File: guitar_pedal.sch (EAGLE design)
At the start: 97 parts, among them P1 RM-065, P2 RM-065, P3 RM-065, U1 LM324NSOIC-14, U2 LM324N, U3 LM386N-3, U4 LM386N-3, U5 LM386N-3

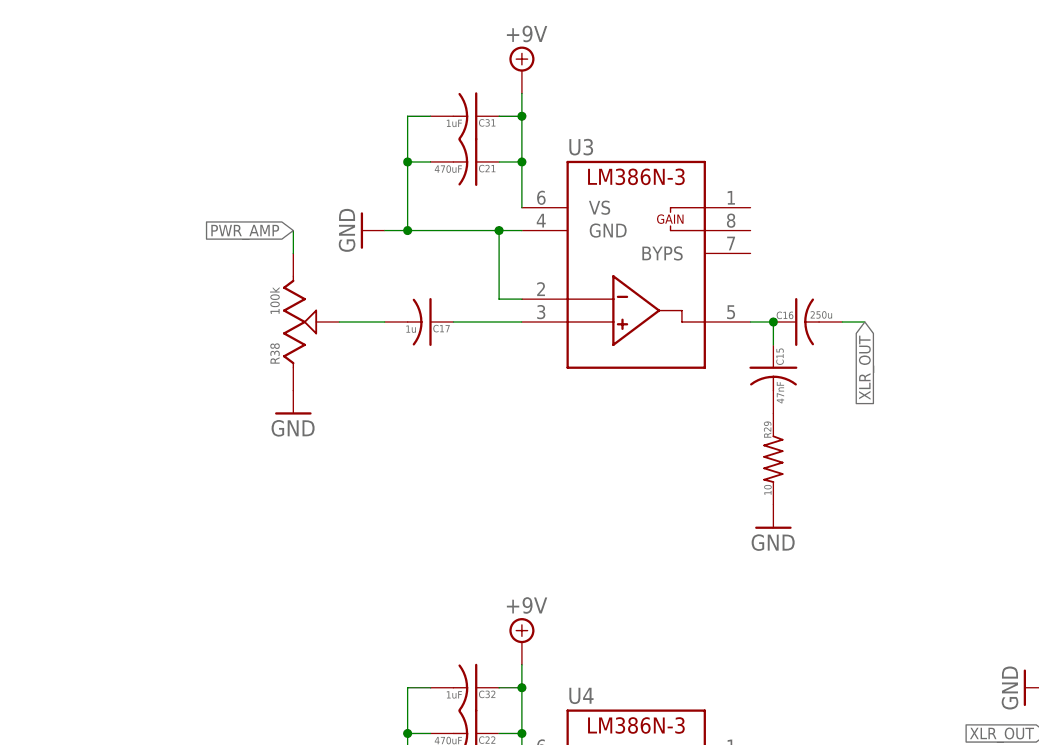
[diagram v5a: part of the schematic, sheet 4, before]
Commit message: Started layout. Placed output components.
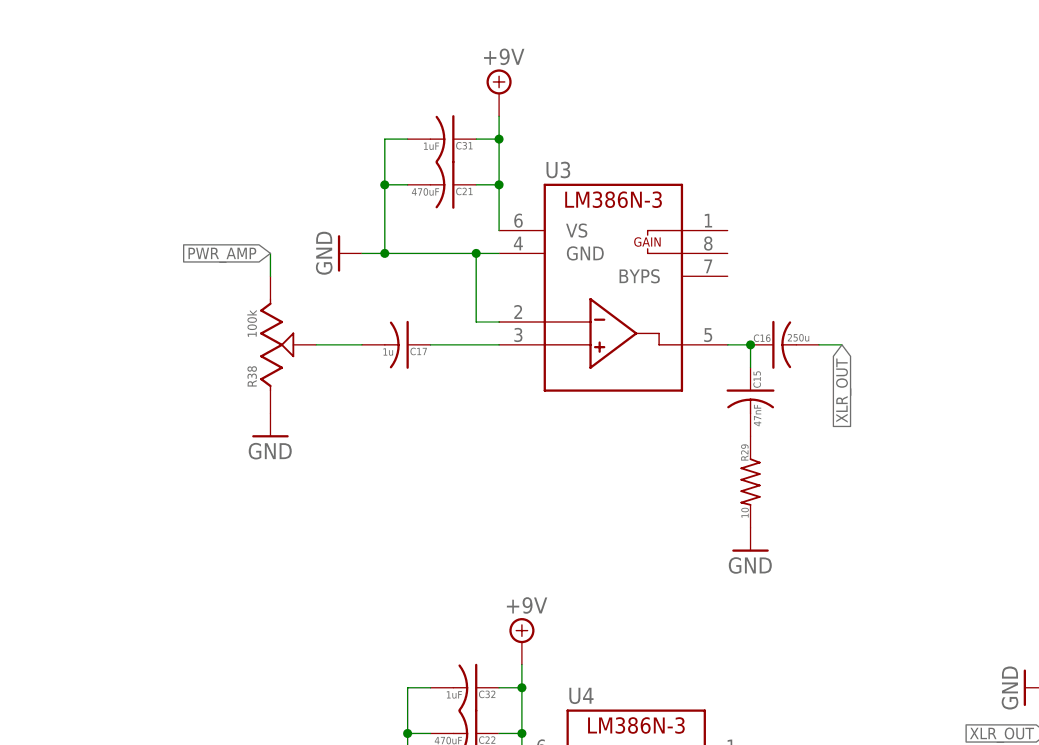
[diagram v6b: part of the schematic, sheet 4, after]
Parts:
- U2: value LM324N -> LM324NSOIC-14; device aarons:LM324N -> aarons:LM324NSOIC-14
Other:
- moved on the sheet: C15, C16, C17, C21, C31, R29, R38, U3
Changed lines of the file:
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@@
 <part name="C26" library="Luke" deviceset="CAP_CAN01" device="" value="470uF"/>
 <part name="U1" library="aarons" deviceset="LM324N" device="SOIC-14" value="LM324NSOIC-14"/>
-<part name="U2" library="aarons" deviceset="LM324N" device=""/>
+<part name="U2" library="aarons" deviceset="LM324N" device="SOIC-14" value="LM324NSOIC-14"/>
 <part name="FRAME2" library="frames" deviceset="FRAME_A_L" device="" value="Power"/>
 <part name="FRAME3" library="frames" deviceset="FRAME_A_L" device="" value="title"/>
@@
 <instance part="GND6" gate="1" x="218.44" y="121.92" rot="MR90"/>
 <instance part="GND7" gate="1" x="210.82" y="106.68" rot="MR90"/>
-<instance part="U3" gate="G$1" x="167.64" y="175.26"/>
-<instance part="GND29" gate="1" x="144.78" y="190.5" rot="R270"/>
-<instance part="C15" gate="G$1" x="190.5" y="175.26"/>
-<instance part="R29" gate="G$1" x="190.5" y="165.1" rot="R270"/>
-<instance part="C16" gate="G$1" x="193.04" y="180.34" rot="R90"/>
-<instance part="GND31" gate="1" x="190.5" y="157.48"/>
-<instance part="SUPPLY5" gate="G$1" x="162.56" y="208.28"/>
-<instance part="C17" gate="G$1" x="152.4" y="180.34" rot="R270"/>
-<instance part="GND32" gate="1" x="137.16" y="170.18"/>
+<instance part="U3" gate="G$1" x="165.1" y="172.72"/>
+<instance part="GND29" gate="1" x="142.24" y="187.96" rot="R270"/>
+<instance part="C15" gate="G$1" x="187.96" y="172.72"/>
+<instance part="R29" gate="G$1" x="187.96" y="162.56" rot="R270"/>
+<instance part="C16" gate="G$1" x="190.5" y="177.8" rot="R90"/>
+<instance part="GND31" gate="1" x="187.96" y="154.94"/>
+<instance part="SUPPLY5" gate="G$1" x="160.02" y="205.74"/>
+<instance part="C17" gate="G$1" x="149.86" y="177.8" rot="R270"/>
+<instance part="GND32" gate="1" x="134.62" y="167.64"/>
 <instance part="U4" gate="G$1" x="167.64" y="114.3"/>
 <instance part="GND33" gate="1" x="144.78" y="127" rot="R270"/>
@@
 <instance part="R36" gate="G$1" x="139.7" y="66.04"/>
 <instance part="R37" gate="G$1" x="137.16" y="119.38"/>
-<instance part="R38" gate="G$1" x="137.16" y="180.34"/>
-<instance part="C21" gate="G$1" x="157.48" y="198.12" rot="R270"/>
-<instance part="C31" gate="G$1" x="157.48" y="203.2" rot="R270"/>
+<instance part="R38" gate="G$1" x="134.62" y="177.8"/>
+<instance part="C21" gate="G$1" x="154.94" y="195.58" rot="R270"/>
+<instance part="C31" gate="G$1" x="154.94" y="200.66" rot="R270"/>
 <instance part="C32" gate="G$1" x="157.48" y="139.7" rot="R270"/>
 <instance part="C33" gate="G$1" x="157.48" y="86.36" rot="R270"/>
@@
 </segment>
 <segment>
-<wire x1="152.4" y1="198.12" x2="149.86" y2="198.12" width="0.1524" layer="91"/>
-<wire x1="149.86" y1="198.12" x2="149.86" y2="190.5" width="0.1524" layer="91"/>
+<wire x1="149.86" y1="195.58" x2="147.32" y2="195.58" width="0.1524" layer="91"/>
+<wire x1="147.32" y1="195.58" x2="147.32" y2="187.96" width="0.1524" layer="91"/>
 <pinref part="U3" gate="G$1" pin="GND"/>
-<wire x1="149.86" y1="190.5" x2="160.02" y2="190.5" width="0.1524" layer="91"/>
+<wire x1="147.32" y1="187.96" x2="157.48" y2="187.96" width="0.1524" layer="91"/>
 <pinref part="U3" gate="G$1" pin="-IN"/>
-<wire x1="160.02" y1="190.5" x2="162.56" y2="190.5" width="0.1524" layer="91"/>
-<wire x1="162.56" y1="182.88" x2="160.02" y2="182.88" width="0.1524" layer="91"/>
-<wire x1="160.02" y1="182.88" x2="160.02" y2="190.5" width="0.1524" layer="91"/>
-<junction x="160.02" y="190.5"/>
+<wire x1="157.48" y1="187.96" x2="160.02" y2="187.96" width="0.1524" layer="91"/>
+<wire x1="160.02" y1="180.34" x2="157.48" y2="180.34" width="0.1524" layer="91"/>
+<wire x1="157.48" y1="180.34" x2="157.48" y2="187.96" width="0.1524" layer="91"/>
+<junction x="157.48" y="187.96"/>
 <pinref part="GND29" gate="1" pin="GND"/>
-<wire x1="149.86" y1="190.5" x2="147.32" y2="190.5" width="0.1524" layer="91"/>
-<junction x="149.86" y="190.5"/>
+<wire x1="147.32" y1="187.96" x2="144.78" y2="187.96" width="0.1524" layer="91"/>
+<junction x="147.32" y="187.96"/>
 <pinref part="C21" gate="G$1" pin="NEG"/>
 <pinref part="C31" gate="G$1" pin="NEG"/>
-<wire x1="152.4" y1="203.2" x2="149.86" y2="203.2" width="0.1524" layer="91"/>
-<wire x1="149.86" y1="203.2" x2="149.86" y2="198.12" width="0.1524" layer="91"/>
-<junction x="149.86" y="198.12"/>
+<wire x1="149.86" y1="200.66" x2="147.32" y2="200.66" width="0.1524" layer="91"/>
+<wire x1="147.32" y1="200.66" x2="147.32" y2="195.58" width="0.1524" layer="91"/>
+<junction x="147.32" y="195.58"/>
 </segment>
 </net>
@@
 <segment>
 <pinref part="U3" gate="G$1" pin="VS"/>
-<wire x1="162.56" y1="193.04" x2="162.56" y2="198.12" width="0.1524" layer="91"/>
+<wire x1="160.02" y1="190.5" x2="160.02" y2="195.58" width="0.1524" layer="91"/>
 <pinref part="SUPPLY5" gate="G$1" pin="+9V"/>
 <pinref part="C21" gate="G$1" pin="POS"/>
-<wire x1="162.56" y1="198.12" x2="162.56" y2="203.2" width="0.1524" layer="91"/>
-<wire x1="162.56" y1="203.2" x2="162.56" y2="205.74" width="0.1524" layer="91"/>
-<wire x1="160.02" y1="198.12" x2="162.56" y2="198.12" width="0.1524" layer="91"/>
-<junction x="162.56" y="198.12"/>
+<wire x1="160.02" y1="195.58" x2="160.02" y2="200.66" width="0.1524" layer="91"/>
+<wire x1="160.02" y1="200.66" x2="160.02" y2="203.2" width="0.1524" layer="91"/>
+<wire x1="157.48" y1="195.58" x2="160.02" y2="195.58" width="0.1524" layer="91"/>
+<junction x="160.02" y="195.58"/>
 <pinref part="C31" gate="G$1" pin="POS"/>
-<wire x1="160.02" y1="203.2" x2="162.56" y2="203.2" width="0.1524" layer="91"/>
-<junction x="162.56" y="203.2"/>
+<wire x1="157.48" y1="200.66" x2="160.02" y2="200.66" width="0.1524" layer="91"/>
+<junction x="160.02" y="200.66"/>
 </segment>
 <segment>
@@
 <segment>
 <pinref part="C16" gate="G$1" pin="NEG"/>
-<wire x1="198.12" y1="180.34" x2="200.66" y2="180.34" width="0.1524" layer="91"/>
-<label x="200.66" y="180.34" size="1.27" layer="95" rot="R270" xref="yes"/>
+<wire x1="195.58" y1="177.8" x2="198.12" y2="177.8" width="0.1524" layer="91"/>
+<label x="198.12" y="177.8" size="1.27" layer="95" rot="R270" xref="yes"/>
 </segment>
 </net>
@@
 <segment>
 <pinref part="U3" gate="G$1" pin="VOUT"/>
-<wire x1="187.96" y1="180.34" x2="190.5" y2="180.34" width="0.1524" layer="91"/>
-<wire x1="190.5" y1="180.34" x2="190.5" y2="177.8" width="0.1524" layer="91"/>
-<junction x="190.5" y="180.34"/>
+<wire x1="185.42" y1="177.8" x2="187.96" y2="177.8" width="0.1524" layer="91"/>
+<wire x1="187.96" y1="177.8" x2="187.96" y2="175.26" width="0.1524" layer="91"/>
+<junction x="187.96" y="177.8"/>
 <pinref part="C15" gate="G$1" pin="POS"/>
 <pinref part="C16" gate="G$1" pin="POS"/>
@@
 <segment>
 <pinref part="U3" gate="G$1" pin="+IN"/>
-<wire x1="162.56" y1="180.34" x2="154.94" y2="180.34" width="0.1524" layer="91"/>
+<wire x1="160.02" y1="177.8" x2="152.4" y2="177.8" width="0.1524" layer="91"/>
 <pinref part="C17" gate="G$1" pin="POS"/>
 </segment>
@@
 <segment>
 <pinref part="C17" gate="G$1" pin="NEG"/>
-<wire x1="142.24" y1="180.34" x2="147.32" y2="180.34" width="0.1524" layer="91"/>
+<wire x1="139.7" y1="177.8" x2="144.78" y2="177.8" width="0.1524" layer="91"/>
 <pinref part="R38" gate="G$1" pin="W"/>
 </segment>
@@
 <net name="PWR_AMP" class="0">
 <segment>
-<wire x1="137.16" y1="187.96" x2="137.16" y2="190.5" width="0.1524" layer="91"/>
-<label x="137.16" y="190.5" size="1.27" layer="95" rot="R180" xref="yes"/>
+<wire x1="134.62" y1="185.42" x2="134.62" y2="187.96" width="0.1524" layer="91"/>
+<label x="134.62" y="187.96" size="1.27" layer="95" rot="R180" xref="yes"/>
 <pinref part="R38" gate="G$1" pin="2"/>
 </segment>

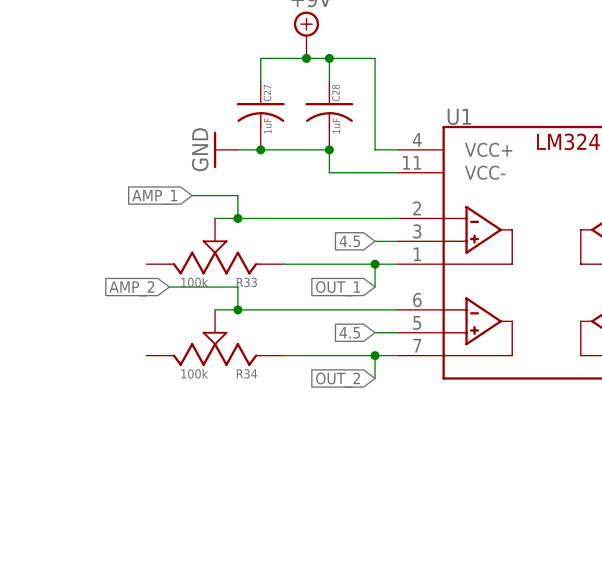
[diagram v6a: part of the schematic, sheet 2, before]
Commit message: Finished laying out the components.
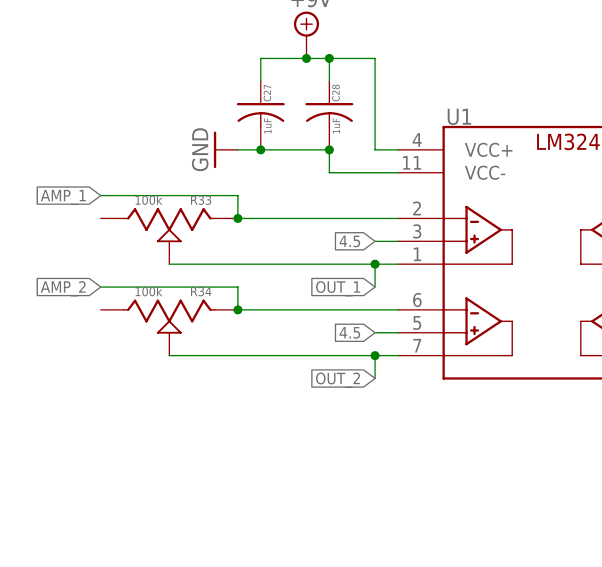
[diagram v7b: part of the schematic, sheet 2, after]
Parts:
- added C34: 1uF, Luke:CAPACITOR0805
- R1, R2: device resistor:R-US_R0805 -> Luke:RESISTOR0805
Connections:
- net 4.5: now also C34.POS
- net AMP_1: now also R33.1; no longer R33.W
- net AMP_2: now also R34.1; no longer R34.W
- net AUDIO_IN_L: now also P3.1; no longer P3.2
- net GND: now also C34.NEG, P3.2; no longer P3.1
- net OUT_1: now also R33.W; no longer R33.1
- net OUT_2: now also R34.W; no longer R34.1
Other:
- moved on the sheet: P3, R33, R34
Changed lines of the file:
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@@
 <part name="GND9" library="supply1" deviceset="GND" device=""/>
 <part name="GND10" library="supply1" deviceset="GND" device=""/>
-<part name="R1" library="resistor" deviceset="R-US_" device="R0805" value="100k"/>
-<part name="R2" library="resistor" deviceset="R-US_" device="R0805" value="100k"/>
+<part name="R1" library="Luke" deviceset="RESISTOR" device="0805" value="100k"/>
+<part name="R2" library="Luke" deviceset="RESISTOR" device="0805" value="100k"/>
 <part name="GND11" library="supply1" deviceset="GND" device=""/>
 <part name="SUPPLY1" library="supply2" deviceset="+9V" device=""/>
@@
 <part name="C32" library="Luke" deviceset="CAPACITOR" device="0805" value="1uF"/>
 <part name="C33" library="Luke" deviceset="CAPACITOR" device="0805" value="1uF"/>
+<part name="C34" library="Luke" deviceset="CAPACITOR" device="0805" value="1uF"/>
+<part name="GND40" library="supply1" deviceset="GND" device=""/>
 </parts>
 <sheets>
@@
 <instance part="GND18" gate="1" x="160.02" y="53.34"/>
 <instance part="R8" gate="G$1" x="172.72" y="68.58" rot="R180"/>
-<instance part="P3" gate="G$1" x="137.16" y="96.52"/>
+<instance part="P3" gate="G$1" x="137.16" y="96.52" rot="MR180"/>
 <instance part="C6" gate="G$1" x="149.86" y="96.52" rot="R90"/>
-<instance part="GND19" gate="1" x="137.16" y="86.36"/>
+<instance part="GND19" gate="1" x="137.16" y="83.82"/>
 <instance part="D6" gate="G$1" x="160.02" y="88.9" rot="R90"/>
 <instance part="GND20" gate="1" x="160.02" y="81.28"/>
@@
 </segment>
 <segment>
-<pinref part="GND19" gate="1" pin="GND"/>
-<pinref part="P3" gate="G$1" pin="1"/>
-</segment>
-<segment>
 <pinref part="GND17" gate="1" pin="GND"/>
 <pinref part="P2" gate="G$1" pin="1"/>
+</segment>
+<segment>
+<pinref part="GND19" gate="1" pin="GND"/>
+<pinref part="P3" gate="G$1" pin="2"/>
+<wire x1="137.16" y1="88.9" x2="137.16" y2="86.36" width="0.1524" layer="91"/>
 </segment>
 </net>
@@
 <net name="AUDIO_IN_L" class="0">
 <segment>
-<wire x1="137.16" y1="104.14" x2="137.16" y2="106.68" width="0.1524" layer="91"/>
-<label x="137.16" y="106.68" size="1.27" layer="95" rot="R180" xref="yes"/>
-<pinref part="P3" gate="G$1" pin="2"/>
+<wire x1="137.16" y1="104.14" x2="134.62" y2="106.68" width="0.1524" layer="91"/>
+<wire x1="134.62" y1="106.68" x2="132.08" y2="106.68" width="0.1524" layer="91"/>
+<label x="132.08" y="106.68" size="1.27" layer="95" rot="R180" xref="yes"/>
+<pinref part="P3" gate="G$1" pin="1"/>
 </segment>
 <segment>
@@
 </segment>
 </net>
-<net name="N$6" class="0">
-<segment>
-<pinref part="C6" gate="G$1" pin="POS"/>
-<pinref part="P3" gate="G$1" pin="W"/>
-<wire x1="142.24" y1="96.52" x2="147.32" y2="96.52" width="0.1524" layer="91"/>
-</segment>
-</net>
 <net name="N$2" class="0">
 <segment>
@@
 <wire x1="165.1" y1="167.64" x2="165.1" y2="172.72" width="0.1524" layer="91"/>
 <junction x="165.1" y="172.72"/>
+</segment>
+</net>
+<net name="N$6" class="0">
+<segment>
+<pinref part="C6" gate="G$1" pin="POS"/>
+<pinref part="P3" gate="G$1" pin="W"/>
+<wire x1="142.24" y1="96.52" x2="147.32" y2="96.52" width="0.1524" layer="91"/>
 </segment>
 </net>
@@
 <instance part="R13" gate="G$1" x="185.42" y="76.2" rot="R180"/>
 <instance part="U1" gate="G$1" x="121.92" y="96.52"/>
-<instance part="R33" gate="G$1" x="96.52" y="109.22" rot="R90"/>
-<instance part="R34" gate="G$1" x="96.52" y="99.06" rot="R90"/>
+<instance part="R33" gate="G$1" x="91.44" y="114.3" rot="MR270"/>
+<instance part="R34" gate="G$1" x="91.44" y="104.14" rot="MR270"/>
 <instance part="R35" gate="G$1" x="185.42" y="109.22" rot="R90"/>
 <instance part="C27" gate="G$1" x="101.6" y="127"/>
@@
 <net name="AMP_1" class="0">
 <segment>
-<label x="93.98" y="116.84" size="1.27" layer="95" rot="R180" xref="yes"/>
+<label x="83.82" y="116.84" size="1.27" layer="95" rot="R180" xref="yes"/>
 <pinref part="U1" gate="G$1" pin="INV_IN_1"/>
-<pinref part="R33" gate="G$1" pin="W"/>
 <wire x1="116.84" y1="114.3" x2="99.06" y2="114.3" width="0.1524" layer="91"/>
-<wire x1="99.06" y1="114.3" x2="96.52" y2="114.3" width="0.1524" layer="91"/>
 <wire x1="99.06" y1="114.3" x2="99.06" y2="116.84" width="0.1524" layer="91"/>
+<wire x1="99.06" y1="116.84" x2="83.82" y2="116.84" width="0.1524" layer="91"/>
+<pinref part="R33" gate="G$1" pin="1"/>
 <junction x="99.06" y="114.3"/>
-<wire x1="99.06" y1="116.84" x2="93.98" y2="116.84" width="0.1524" layer="91"/>
 </segment>
 </net>
@@
 <segment>
 <pinref part="U1" gate="G$1" pin="OUT_1"/>
-<pinref part="R33" gate="G$1" pin="1"/>
-<wire x1="104.14" y1="109.22" x2="114.3" y2="109.22" width="0.1524" layer="91"/>
 <label x="114.3" y="106.68" size="1.27" layer="95" rot="R180" xref="yes"/>
 <wire x1="114.3" y1="109.22" x2="116.84" y2="109.22" width="0.1524" layer="91"/>
 <wire x1="114.3" y1="106.68" x2="114.3" y2="109.22" width="0.1524" layer="91"/>
+<pinref part="R33" gate="G$1" pin="W"/>
+<wire x1="91.44" y1="109.22" x2="114.3" y2="109.22" width="0.1524" layer="91"/>
 <junction x="114.3" y="109.22"/>
 </segment>
@@
 <label x="114.3" y="96.52" size="1.27" layer="95" rot="R180" xref="yes"/>
 <pinref part="U1" gate="G$1" pin="OUT_2"/>
-<pinref part="R34" gate="G$1" pin="1"/>
-<wire x1="104.14" y1="99.06" x2="114.3" y2="99.06" width="0.1524" layer="91"/>
 <wire x1="114.3" y1="99.06" x2="116.84" y2="99.06" width="0.1524" layer="91"/>
 <wire x1="114.3" y1="96.52" x2="114.3" y2="99.06" width="0.1524" layer="91"/>
+<pinref part="R34" gate="G$1" pin="W"/>
+<wire x1="91.44" y1="99.06" x2="114.3" y2="99.06" width="0.1524" layer="91"/>
 <junction x="114.3" y="99.06"/>
 </segment>
@@
 <net name="AMP_2" class="0">
 <segment>
-<label x="91.44" y="106.68" size="1.27" layer="95" rot="R180" xref="yes"/>
+<label x="83.82" y="106.68" size="1.27" layer="95" rot="R180" xref="yes"/>
 <pinref part="U1" gate="G$1" pin="INV_IN_2"/>
-<pinref part="R34" gate="G$1" pin="W"/>
 <wire x1="116.84" y1="104.14" x2="99.06" y2="104.14" width="0.1524" layer="91"/>
-<wire x1="99.06" y1="104.14" x2="96.52" y2="104.14" width="0.1524" layer="91"/>
 <wire x1="99.06" y1="104.14" x2="99.06" y2="106.68" width="0.1524" layer="91"/>
+<wire x1="99.06" y1="106.68" x2="83.82" y2="106.68" width="0.1524" layer="91"/>
+<pinref part="R34" gate="G$1" pin="1"/>
 <junction x="99.06" y="104.14"/>
-<wire x1="99.06" y1="106.68" x2="91.44" y2="106.68" width="0.1524" layer="91"/>
 </segment>
 </net>
@@
 <instance part="C2" gate="G$1" x="157.48" y="114.3"/>
 <instance part="F1" gate="G$1" x="116.84" y="121.92"/>
+<instance part="C34" gate="G$1" x="182.88" y="99.06"/>
+<instance part="GND40" gate="1" x="182.88" y="91.44"/>
 </instances>
 <busses>
@@
 <wire x1="142.24" y1="106.68" x2="142.24" y2="109.22" width="0.1524" layer="91"/>
 </segment>
+<segment>
+<pinref part="C34" gate="G$1" pin="NEG"/>
+<pinref part="GND40" gate="1" pin="GND"/>
+</segment>
 </net>
 <net name="N$1" class="0">
@@
 <wire x1="172.72" y1="109.22" x2="172.72" y2="106.68" width="0.1524" layer="91"/>
 <wire x1="172.72" y1="106.68" x2="172.72" y2="104.14" width="0.1524" layer="91"/>
-<wire x1="172.72" y1="106.68" x2="177.8" y2="106.68" width="0.1524" layer="91"/>
+<wire x1="172.72" y1="106.68" x2="182.88" y2="106.68" width="0.1524" layer="91"/>
 <junction x="172.72" y="106.68"/>
-<label x="177.8" y="106.68" size="1.4224" layer="95" xref="yes"/>
-</segment>
-</net>
+<label x="187.96" y="106.68" size="1.4224" layer="95" xref="yes"/>
+<pinref part="C34" gate="G$1" pin="POS"/>
+<wire x1="182.88" y1="106.68" x2="187.96" y2="106.68" width="0.1524" layer="91"/>
+<wire x1="182.88" y1="101.6" x2="182.88" y2="106.68" width="0.1524" layer="91"/>
+<junction x="182.88" y="106.68"/>
+</segment>
+</net>
